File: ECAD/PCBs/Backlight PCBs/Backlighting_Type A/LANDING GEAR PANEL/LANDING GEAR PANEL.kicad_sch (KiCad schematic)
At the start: 48 parts

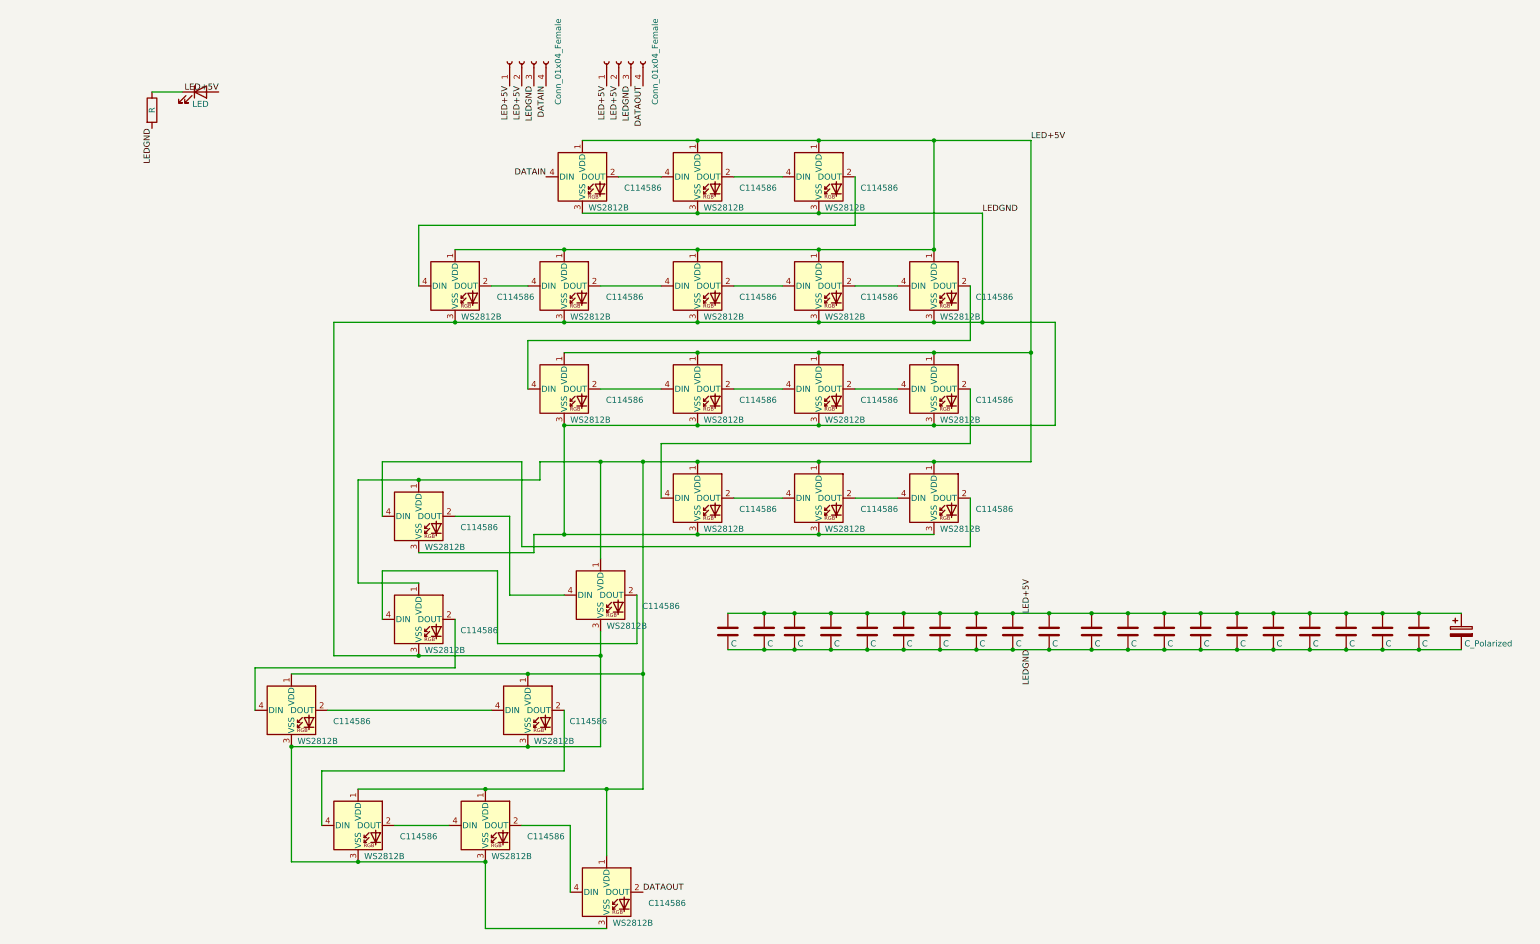
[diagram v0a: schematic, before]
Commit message: Drawing Sheet & Silkscreen update - Backlight Panels (Fc thru Spin)
1:  Updated/Relinked Drawing Sheet for both PCB and Schematics
2:  Standardized Silkscreen (if required)

Finished Remaining Backlighting Type A & Type B PCBs.....
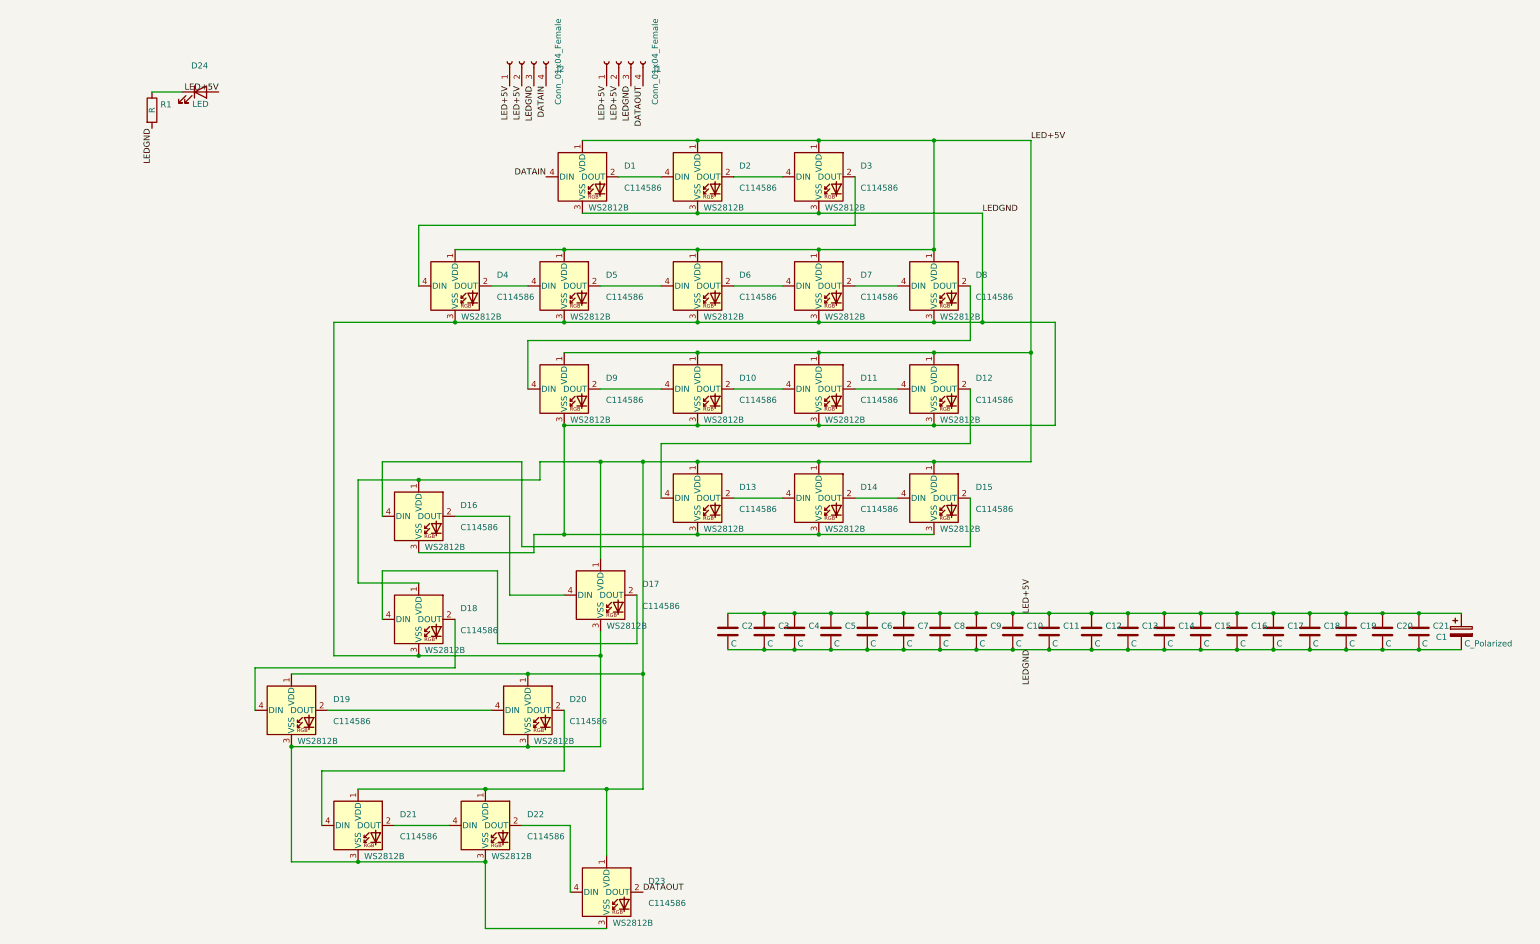
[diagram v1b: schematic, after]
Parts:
- gave numbers to parts that had none: 48
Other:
- title: (none) -> LANDING GEAR PANEL

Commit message: KiCad 7 Transition - LANDING GEAR Panel
PCB and Schematic standardization
Updated silkscreen text
Adjusted traces to prevent conflicts
Add Testpoints
Recompiled assets and manufacturing files
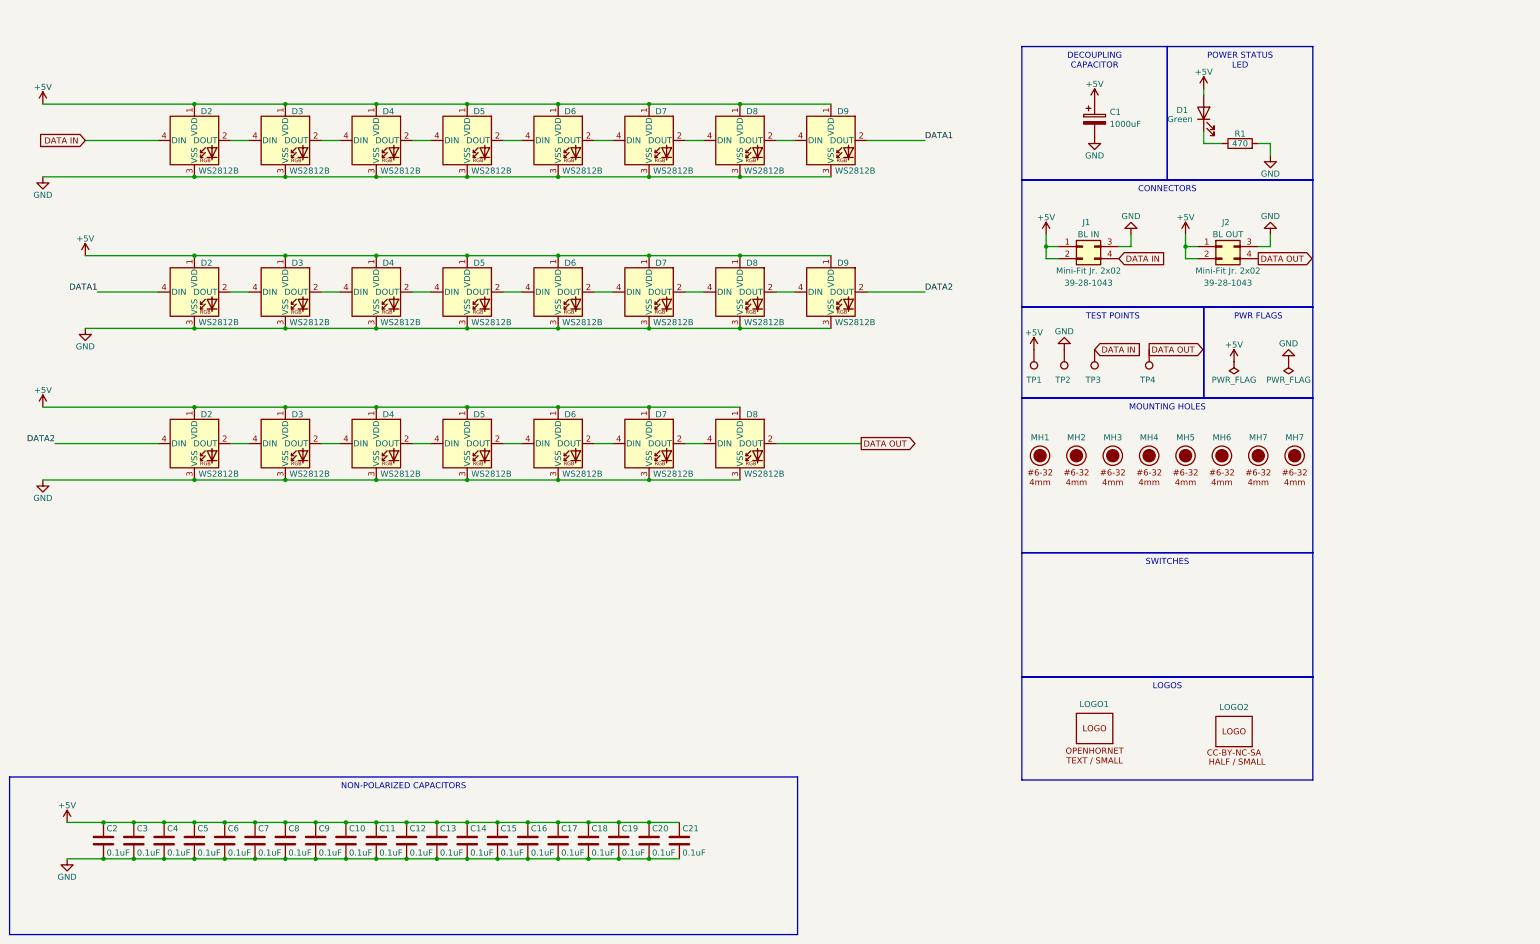
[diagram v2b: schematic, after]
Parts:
- removed C1: C_Polarized, OH_Footprints:CP_Elec_8x10, symbol Device:C_Polarized
- removed C10, C11, C12, C13, C14, C15, C16, C17, C18, C19, C2, C20, C21, C3, C4, C5, C6, C7, C8, C9: C, OH_Footprints:C_0603_1608Metric, symbol Device:C
- removed D1, D10, D11, D12, D13, D14, D15, D16, D17, D18, D19, D2, D20, D21, D22, D23, D3, D4, D5, D6, D7, D8, D9: WS2812B, OH_Footprints:LED_WS2812B_PLCC4_5.0x5.0mm_P3.2mm, symbol LED:WS2812B
- removed D24: LED, OH_Footprints:LED_D3.0mm, symbol Device:LED
- removed J1, J2: Conn_01x04_Female, OH_Footprints:Molex_Mini-Fit_Jr_5566-04A_2x02_P4.20mm_Vertical, symbol Connector:Conn_01x04_Female
- removed R1: R, OH_Footprints:R_0603_1608Metric, symbol Device:R
- added C1: 1000uF, OH_Footprints:CP_Elec_8x10, symbol OH_Symbols:Capacitor_Polarized_8x10_1000uF
- added C10, C11, C12, C13, C14, C15, C16, C17, C18, C19, C2, C20, C21, C3, C4, C5, C6, C7, C8, C9: 0.1uF, OH_Footprints:C_0603_1608Metric, symbol OH_Symbols:Capacitor_0603_0.1uF
- added D1: Green, OH_Footprints:LED_D3.0mm, symbol OH_Symbols:LED_3.0mm_Green
- added D2 (x3), D3 (x3), D4 (x3), D5 (x3), D6 (x3), D7 (x3), D8 (x3), D9 (x2): WS2812B, OH_Footprints:LED_WS2812B_PLCC4_5.0x5.0mm_P3.2mm, symbol OH_Symbols:WS2812B
- added J1, J2: Mini-Fit Jr. 2x02, OH_Footprints:Molex_Mini-Fit_Jr_5566-04A_2x02_P4.20mm_Vertical, symbol OH_Symbols:Molex_Mini-Fit_Jr._2x02
- added LOGO1: LOGO, OH_Footprints:LOGO_OH_Text_Small, symbol OH_Symbols:LOGO_OpenHornet_Text_Small
- added LOGO2: LOGO, OH_Footprints:LOGO_CC-BY-NC-SA_Half_Small, symbol OH_Symbols:LOGO_License_Half_Small
- added MH1, MH2, MH3, MH4, MH5, MH6, MH7 (x2): 6x32 / 4mm, OH_Footprints:MountingHole_6-32_PHS, symbol OH_Symbols:MountingHole_6x32_PHS
- added R1: 470, OH_Footprints:R_0603_1608Metric, symbol OH_Symbols:Resistor_0603_470Ω
- added TP1, TP2, TP3, TP4: TestPoint, OH_Footprints:TestPoint_THTPad_D1.5mm_Drill0.7mm, symbol OH_Symbols:TestPoint
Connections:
- new net: D8.2 (DOUT), D9.4 (DIN) (x2)
- new net: D7.2 (DOUT), D8.4 (DIN) (x3)
- new net: D6.2 (DOUT), D7.4 (DIN) (x3)
- new net: D5.2 (DOUT), D6.4 (DIN) (x3)
- new net: D4.2 (DOUT), D5.4 (DIN) (x3)
- new net: D3.2 (DOUT), D4.4 (DIN) (x3)
- new net: D2.2 (DOUT), D3.4 (DIN) (x3)
- new net: D1.1 (K), R1.1
- new net +5V: C1.1, C10.1, C11.1, C12.1, C13.1, C14.1, C15.1, C16.1, C17.1, C18.1, C19.1, C2.1, C20.1, C21.1, C3.1, C4.1, C5.1, C6.1, C7.1, C8.1, C9.1, D1.2 (A), D2.1 (VDD), D2.1 (VDD), D2.1 (VDD), D3.1 (VDD), D3.1 (VDD), D3.1 (VDD), D4.1 (VDD), D4.1 (VDD), D4.1 (VDD), D5.1 (VDD), D5.1 (VDD), D5.1 (VDD), D6.1 (VDD), D6.1 (VDD), D6.1 (VDD), D7.1 (VDD), D7.1 (VDD), D7.1 (VDD), D8.1 (VDD), D8.1 (VDD), D8.1 (VDD), D9.1 (VDD), D9.1 (VDD), J1.1 (Pin_1), J1.2 (Pin_3), J2.1 (Pin_1), J2.2 (Pin_3), TP1.1
- new net DATA IN: D2.4 (DIN), J1.4 (Pin_4), TP3.1
- new net DATA OUT: D8.2 (DOUT), J2.4 (Pin_4), TP4.1
- new net DATA1: D2.4 (DIN), D9.2 (DOUT)
- new net DATA2: D2.4 (DIN), D9.2 (DOUT)
- new net GND: C1.2, C10.2, C11.2, C12.2, C13.2, C14.2, C15.2, C16.2, C17.2, C18.2, C19.2, C2.2, C20.2, C21.2, C3.2, C4.2, C5.2, C6.2, C7.2, C8.2, C9.2, D2.3 (VSS), D2.3 (VSS), D2.3 (VSS), D3.3 (VSS), D3.3 (VSS), D3.3 (VSS), D4.3 (VSS), D4.3 (VSS), D4.3 (VSS), D5.3 (VSS), D5.3 (VSS), D5.3 (VSS), D6.3 (VSS), D6.3 (VSS), D6.3 (VSS), D7.3 (VSS), D7.3 (VSS), D7.3 (VSS), D8.3 (VSS), D8.3 (VSS), D8.3 (VSS), D9.3 (VSS), D9.3 (VSS), J1.3 (Pin_2), J2.3 (Pin_2), R1.2, TP2.1
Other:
- company: (none) -> www.openhornet.com
